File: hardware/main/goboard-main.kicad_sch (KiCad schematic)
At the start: 11 parts, among them J1 USB_C_Receptacle_USB2.0, J2 Conn_02x05_Top_Bottom, J3 Conn_01x01, J4 Conn_01x04, SW11 SW_Push, SW30 SW_DP3T

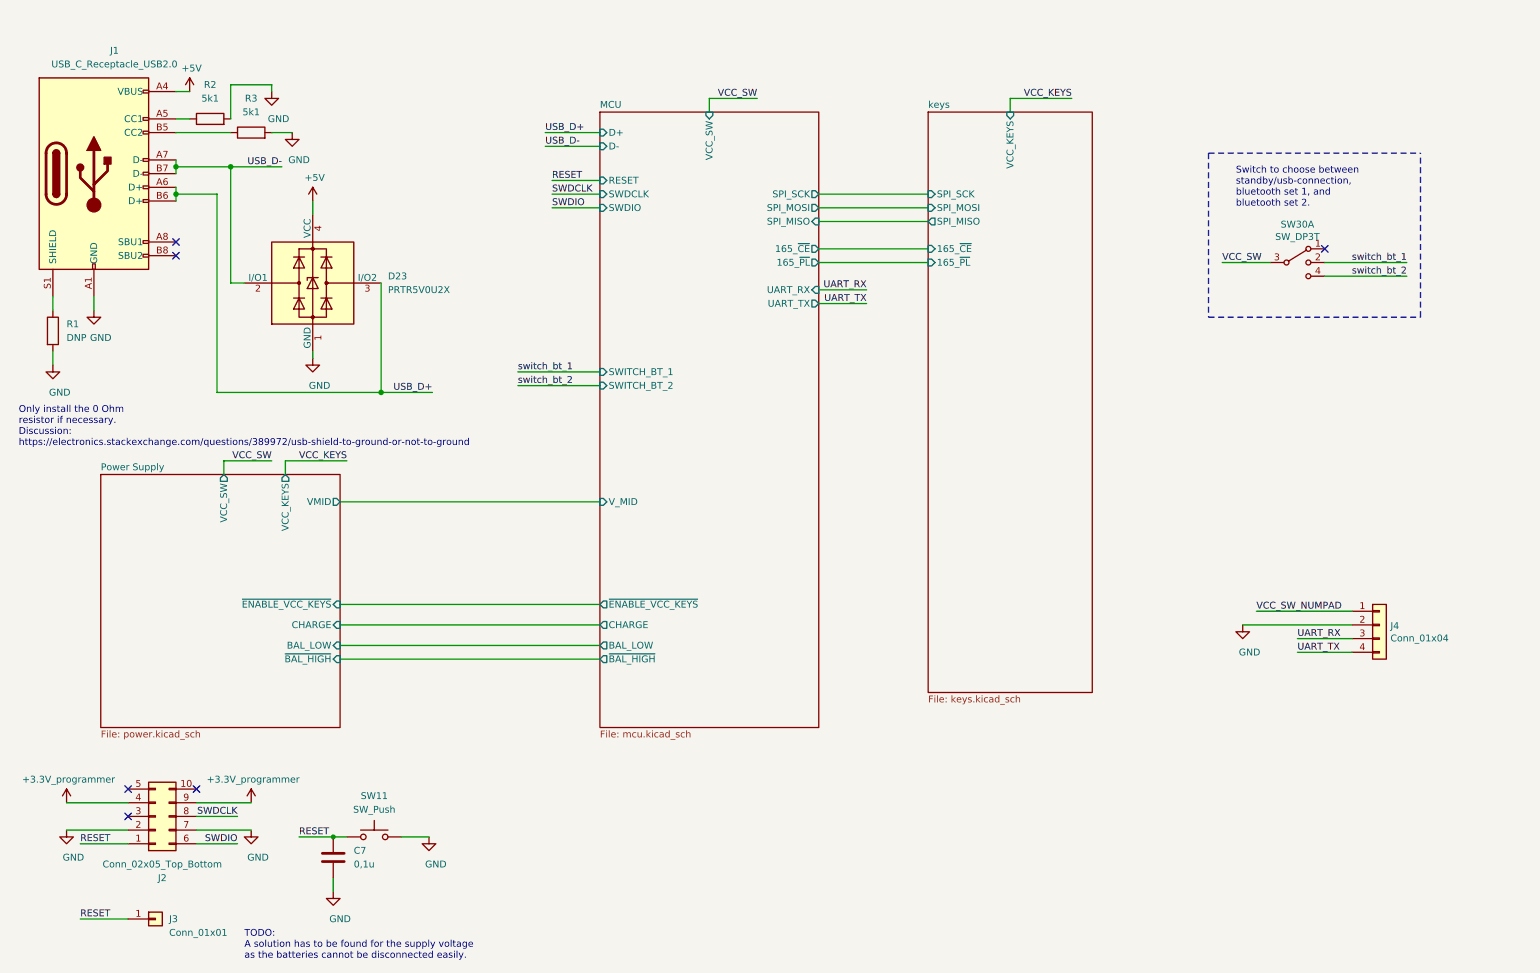
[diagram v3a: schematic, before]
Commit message: Rework the connection to the numpad
Changes:
- The UART lines now have a protection circuit
- The power supply line of the numpad can be switched on and off by the MCU.
- An Id-line is added so that the MCU can detect when the numpad is
  connected.
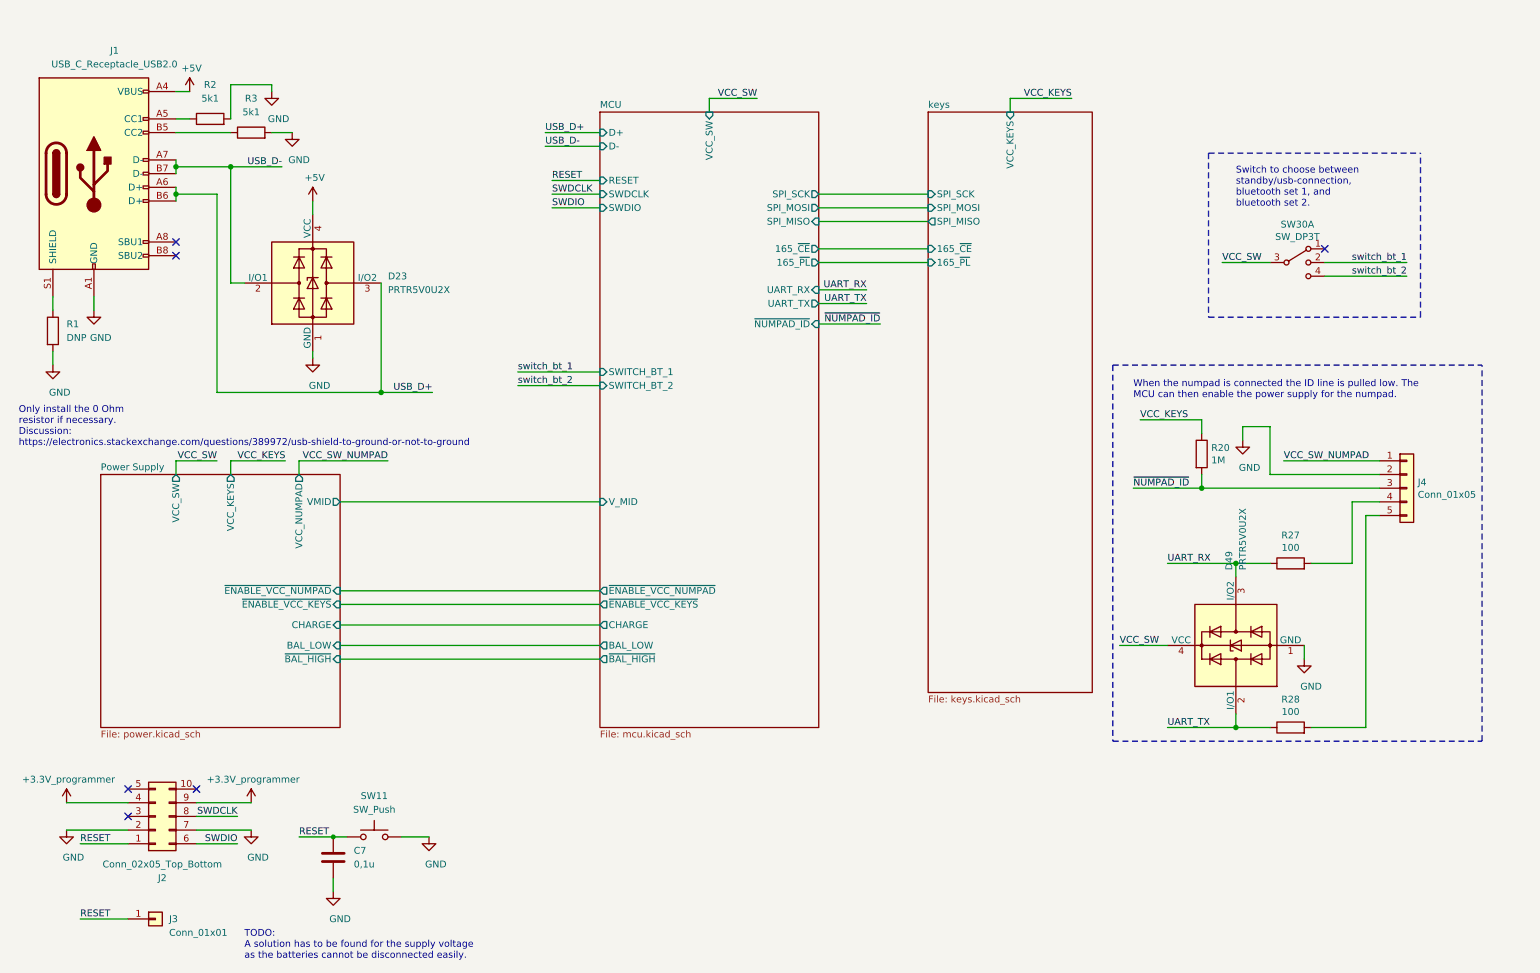
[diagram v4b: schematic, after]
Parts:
- removed J4: Conn_01x04, symbol Connector_Generic:Conn_01x04
- added D49: PRTR5V0U2X, Package_TO_SOT_SMD:SOT-143, symbol Power_Protection:PRTR5V0U2X
- added J4: Conn_01x05, Connector_PinHeader_2.54mm:PinHeader_1x05_P2.54mm_Vertical, symbol Connector_Generic:Conn_01x05
- added R20: 1M, Resistor_SMD:R_0603_1608Metric_Pad0.98x0.95mm_HandSolder, symbol Device:R
- added R27, R28: 100, Resistor_SMD:R_0603_1608Metric_Pad0.98x0.95mm_HandSolder, symbol Device:R
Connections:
- net GND: now also D49.1 (GND), J4.2 (Pin_2)
- net UART_RX: now also D49.3 (I/O2), R27.1
- net UART_TX: now also D49.2 (I/O1), R28.1
- net VCC_KEYS: now also R20.1
- net VCC_SW: now also D49.4 (VCC)
- net VCC_SW_NUMPAD: now also J4.1 (Pin_1)
- new net: J4.4 (Pin_4), R27.2
- new net: J4.5 (Pin_5), R28.2
- new net ~NUMPAD_ID: J4.3 (Pin_3), R20.2
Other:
- sheet MCU ports: added ~ENABLE_VCC_NUMPAD, ~NUMPAD_ID; removed none
- sheet Power Supply ports: added VCC_NUMPAD, ~ENABLE_VCC_NUMPAD; removed none
- note added: "When the numpad is connected the ID line is pulled low. The MCU can then enable the power supply for the numpad."

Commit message: WIP: Design of PCB
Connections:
- net UART_RX: no longer D49.3 (I/O2)
- net UART_TX: no longer D49.2 (I/O1)
- net at J4.4 (Pin_4), R27.2: now also D49.2 (I/O1)
- net at J4.5 (Pin_5), R28.2: now also D49.3 (I/O2)
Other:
- moved on the sheet: D49, R27, R28
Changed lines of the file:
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@@
   (junction (at 80.01 91.44) (diameter 1.016) (color 0 0 0 0))
   (junction (at 232.41 109.22) (diameter 1.016) (color 0 0 0 0))
-  (junction (at 238.76 123.19) (diameter 1.016) (color 0 0 0 0))
-  (junction (at 238.76 153.67) (diameter 1.016) (color 0 0 0 0))
+  (junction (at 246.38 123.19) (diameter 1.016) (color 0 0 0 0))
+  (junction (at 246.38 153.67) (diameter 1.016) (color 0 0 0 0))
   (no_connect (at 33.02 165.1))
   (no_connect (at 33.02 170.18))
@@
     (stroke (width 0) (type solid) (color 0 0 0 0))
   )
-  (wire (pts (xy 217.17 138.43) (xy 226.06 138.43))
-    (stroke (width 0) (type solid) (color 0 0 0 0))
-  )
   (wire (pts (xy 219.71 109.22) (xy 232.41 109.22))
     (stroke (width 0) (type solid) (color 0 0 0 0))
@@
     (stroke (width 0) (type solid) (color 0 0 0 0))
   )
-  (wire (pts (xy 226.06 123.19) (xy 238.76 123.19))
-    (stroke (width 0) (type solid) (color 0 0 0 0))
-  )
-  (wire (pts (xy 226.06 153.67) (xy 238.76 153.67))
+  (wire (pts (xy 226.06 123.19) (xy 236.22 123.19))
+    (stroke (width 0) (type solid) (color 0 0 0 0))
+  )
+  (wire (pts (xy 226.06 138.43) (xy 233.68 138.43))
+    (stroke (width 0) (type solid) (color 0 0 0 0))
+  )
+  (wire (pts (xy 226.06 153.67) (xy 236.22 153.67))
     (stroke (width 0) (type solid) (color 0 0 0 0))
   )
@@
     (stroke (width 0) (type solid) (color 0 0 0 0))
   )
-  (wire (pts (xy 238.76 123.19) (xy 238.76 125.73))
-    (stroke (width 0) (type solid) (color 0 0 0 0))
-  )
-  (wire (pts (xy 238.76 123.19) (xy 245.11 123.19))
-    (stroke (width 0) (type solid) (color 0 0 0 0))
-  )
-  (wire (pts (xy 238.76 151.13) (xy 238.76 153.67))
-    (stroke (width 0) (type solid) (color 0 0 0 0))
-  )
-  (wire (pts (xy 238.76 153.67) (xy 245.11 153.67))
-    (stroke (width 0) (type solid) (color 0 0 0 0))
-  )
   (wire (pts (xy 240.03 97.79) (xy 240.03 100.33))
     (stroke (width 0) (type solid) (color 0 0 0 0))
@@
     (stroke (width 0) (type solid) (color 0 0 0 0))
   )
+  (wire (pts (xy 243.84 123.19) (xy 246.38 123.19))
+    (stroke (width 0) (type solid) (color 0 0 0 0))
+  )
+  (wire (pts (xy 243.84 153.67) (xy 246.38 153.67))
+    (stroke (width 0) (type solid) (color 0 0 0 0))
+  )
   (wire (pts (xy 245.11 97.79) (xy 245.11 106.68))
     (stroke (width 0) (type solid) (color 0 0 0 0))
@@
     (stroke (width 0) (type solid) (color 0 0 0 0))
   )
+  (wire (pts (xy 246.38 123.19) (xy 246.38 125.73))
+    (stroke (width 0) (type solid) (color 0 0 0 0))
+  )
+  (wire (pts (xy 246.38 123.19) (xy 260.35 123.19))
+    (stroke (width 0) (type solid) (color 0 0 0 0))
+  )
+  (wire (pts (xy 246.38 151.13) (xy 246.38 153.67))
+    (stroke (width 0) (type solid) (color 0 0 0 0))
+  )
+  (wire (pts (xy 246.38 153.67) (xy 262.89 153.67))
+    (stroke (width 0) (type solid) (color 0 0 0 0))
+  )
   (wire (pts (xy 247.65 104.14) (xy 265.43 104.14))
     (stroke (width 0) (type solid) (color 0 0 0 0))
   )
-  (wire (pts (xy 251.46 138.43) (xy 251.46 140.97))
-    (stroke (width 0) (type solid) (color 0 0 0 0))
-  )
-  (wire (pts (xy 252.73 123.19) (xy 260.35 123.19))
-    (stroke (width 0) (type solid) (color 0 0 0 0))
-  )
   (wire (pts (xy 255.27 67.31) (xy 270.51 67.31))
     (stroke (width 0) (type solid) (color 0 0 0 0))
@@
     (stroke (width 0) (type solid) (color 0 0 0 0))
   )
+  (wire (pts (xy 259.08 138.43) (xy 259.08 140.97))
+    (stroke (width 0) (type solid) (color 0 0 0 0))
+  )
   (wire (pts (xy 260.35 111.76) (xy 265.43 111.76))
     (stroke (width 0) (type solid) (color 0 0 0 0))
@@
     (stroke (width 0) (type solid) (color 0 0 0 0))
   )
-  (wire (pts (xy 262.89 153.67) (xy 252.73 153.67))
-    (stroke (width 0) (type solid) (color 0 0 0 0))
-  )
   (wire (pts (xy 265.43 114.3) (xy 262.89 114.3))
     (stroke (width 0) (type solid) (color 0 0 0 0))
   )
-  (polyline (pts (xy 215.9 86.36) (xy 215.9 156.21))
+  (polyline (pts (xy 218.44 86.36) (xy 218.44 156.21))
     (stroke (width 0) (type dash) (color 0 0 0 0))
   )
-  (polyline (pts (xy 215.9 86.36) (xy 284.48 86.36))
+  (polyline (pts (xy 218.44 86.36) (xy 284.48 86.36))
     (stroke (width 0) (type dash) (color 0 0 0 0))
   )
-  (polyline (pts (xy 215.9 156.21) (xy 284.48 156.21))
+  (polyline (pts (xy 218.44 156.21) (xy 284.48 156.21))
     (stroke (width 0) (type dash) (color 0 0 0 0))
   )
@@
   )
   (text "When the numpad is connected the ID line is pulled low. The\nMCU can then enable the power supply for the numpad."
-    (at 219.71 92.71 0)
+    (at 220.98 92.71 0)
     (effects (font (size 1.27 1.27)) (justify left bottom))
   )
@@
     (effects (font (size 1.27 1.27)) (justify right bottom))
   )
-  (label "VCC_SW" (at 217.17 138.43 0)
-    (effects (font (size 1.27 1.27)) (justify left bottom))
-  )
   (label "~NUMPAD_ID" (at 219.71 109.22 0)
     (effects (font (size 1.27 1.27)) (justify left bottom))
@@
   )
   (label "UART_RX" (at 226.06 123.19 0)
+    (effects (font (size 1.27 1.27)) (justify left bottom))
+  )
+  (label "VCC_SW" (at 226.06 138.43 0)
     (effects (font (size 1.27 1.27)) (justify left bottom))
   )
@@
     )
   )
-  (symbol (lib_id "power:GND") (at 251.46 140.97 0) (unit 1)
-    (in_bom yes) (on_board yes)
-    (property "Reference" "#PWR0123" (id 0) (at 251.46 147.32 0)
-      (effects (font (size 1.27 1.27)) hide)
-    )
-    (property "Value" "GND" (id 1) (at 252.73 146.05 0))
-    (property "Footprint" "" (id 2) (at 251.46 140.97 0)
-      (effects (font (size 1.27 1.27)) hide)
-    )
-    (property "Datasheet" "" (id 3) (at 251.46 140.97 0)
+  (symbol (lib_id "power:GND") (at 259.08 140.97 0) (unit 1)
+    (in_bom yes) (on_board yes)
+    (property "Reference" "#PWR0123" (id 0) (at 259.08 147.32 0)
+      (effects (font (size 1.27 1.27)) hide)
+    )
+    (property "Value" "GND" (id 1) (at 260.35 146.05 0))
+    (property "Footprint" "" (id 2) (at 259.08 140.97 0)
+      (effects (font (size 1.27 1.27)) hide)
+    )
+    (property "Datasheet" "" (id 3) (at 259.08 140.97 0)
       (effects (font (size 1.27 1.27)) hide)
     )
@@
     )
   )
-  (symbol (lib_id "Device:R") (at 248.92 123.19 90) (unit 1)
-    (in_bom yes) (on_board yes)
-    (property "Reference" "R27" (id 0) (at 248.92 117.9638 90))
-    (property "Value" "100" (id 1) (at 248.92 120.2625 90))
-    (property "Footprint" "Resistor_SMD:R_0603_1608Metric_Pad0.98x0.95mm_HandSolder" (id 2) (at 248.92 124.968 90)
-      (effects (font (size 1.27 1.27)) hide)
-    )
-    (property "Datasheet" "~" (id 3) (at 248.92 123.19 0)
-      (effects (font (size 1.27 1.27)) hide)
-    )
-  )
-  (symbol (lib_id "Device:R") (at 248.92 153.67 90) (unit 1)
-    (in_bom yes) (on_board yes)
-    (property "Reference" "R28" (id 0) (at 248.92 148.4438 90))
-    (property "Value" "100" (id 1) (at 248.92 150.7425 90))
-    (property "Footprint" "Resistor_SMD:R_0603_1608Metric_Pad0.98x0.95mm_HandSolder" (id 2) (at 248.92 155.448 90)
-      (effects (font (size 1.27 1.27)) hide)
-    )
-    (property "Datasheet" "~" (id 3) (at 248.92 153.67 0)
+  (symbol (lib_id "Device:R") (at 240.03 123.19 90) (unit 1)
+    (in_bom yes) (on_board yes)
+    (property "Reference" "R27" (id 0) (at 240.03 117.9638 90))
+    (property "Value" "100" (id 1) (at 240.03 120.2625 90))
+    (property "Footprint" "Resistor_SMD:R_0603_1608Metric_Pad0.98x0.95mm_HandSolder" (id 2) (at 240.03 124.968 90)
+      (effects (font (size 1.27 1.27)) hide)
+    )
+    (property "Datasheet" "~" (id 3) (at 240.03 123.19 0)
+      (effects (font (size 1.27 1.27)) hide)
+    )
+  )
+  (symbol (lib_id "Device:R") (at 240.03 153.67 90) (unit 1)
+    (in_bom yes) (on_board yes)
+    (property "Reference" "R28" (id 0) (at 240.03 148.4438 90))
+    (property "Value" "100" (id 1) (at 240.03 150.7425 90))
+    (property "Footprint" "Resistor_SMD:R_0603_1608Metric_Pad0.98x0.95mm_HandSolder" (id 2) (at 240.03 155.448 90)
+      (effects (font (size 1.27 1.27)) hide)
+    )
+    (property "Datasheet" "~" (id 3) (at 240.03 153.67 0)
       (effects (font (size 1.27 1.27)) hide)
     )
@@
     )
   )
-  (symbol (lib_id "Power_Protection:PRTR5V0U2X") (at 238.76 138.43 90) (unit 1)
-    (in_bom yes) (on_board yes)
-    (property "Reference" "D49" (id 0) (at 237.49 124.46 0)
-      (effects (font (size 1.27 1.27)) (justify left))
-    )
-    (property "Value" "PRTR5V0U2X" (id 1) (at 240.03 124.46 0)
-      (effects (font (size 1.27 1.27)) (justify left))
-    )
-    (property "Footprint" "Package_TO_SOT_SMD:SOT-143" (id 2) (at 238.76 136.906 0)
-      (effects (font (size 1.27 1.27)) hide)
-    )
-    (property "Datasheet" "https://assets.nexperia.com/documents/data-sheet/PRTR5V0U2X.pdf" (id 3) (at 238.76 136.906 0)
-      (effects (font (size 1.27 1.27)) hide)
-    )
-    (property "Mouser" " 771-PRTR5V0U2X-T/R " (id 4) (at 238.76 138.43 0)
-      (effects (font (size 1.27 1.27)) hide)
-    )
-    (property "Part Name" "PRTR5V0U2X,215" (id 5) (at 238.76 138.43 0)
-      (effects (font (size 1.27 1.27)) hide)
-    )
+  (symbol (lib_id "Power_Protection:PRTR5V0U2X") (at 246.38 138.43 90) (mirror x) (unit 1)
+    (in_bom yes) (on_board yes)
+    (property "Reference" "D49" (id 0) (at 245.11 152.4 0)
+      (effects (font (size 1.27 1.27)) (justify left))
+    )
+    (property "Value" "PRTR5V0U2X" (id 1) (at 247.65 152.4 0)
+      (effects (font (size 1.27 1.27)) (justify left))
+    )
+    (property "Footprint" "Package_TO_SOT_SMD:SOT-143" (id 2) (at 246.38 139.954 0)
+      (effects (font (size 1.27 1.27)) hide)
+    )
+    (property "Datasheet" "https://assets.nexperia.com/documents/data-sheet/PRTR5V0U2X.pdf" (id 3) (at 246.38 139.954 0)
+      (effects (font (size 1.27 1.27)) hide)
+    )
+    (property "Mouser" " 771-PRTR5V0U2X-T/R " (id 4) (at 246.38 138.43 0)
+      (effects (font (size 1.27 1.27)) hide)
+    )
+    (property "Part Name" "PRTR5V0U2X,215" (id 5) (at 246.38 138.43 0)
+      (effects (font (size 1.27 1.27)) hide)
+    )

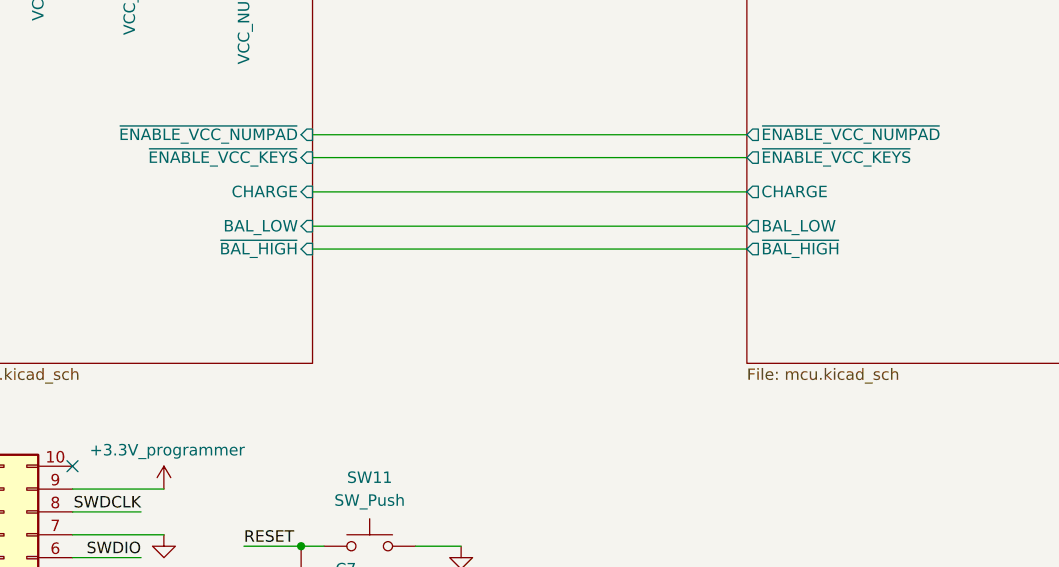
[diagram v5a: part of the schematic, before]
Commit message: Re-add USB voltage sense circuit
Due to firmware limitations the USB voltage cannot be used directly for
waking up the microcontroller.
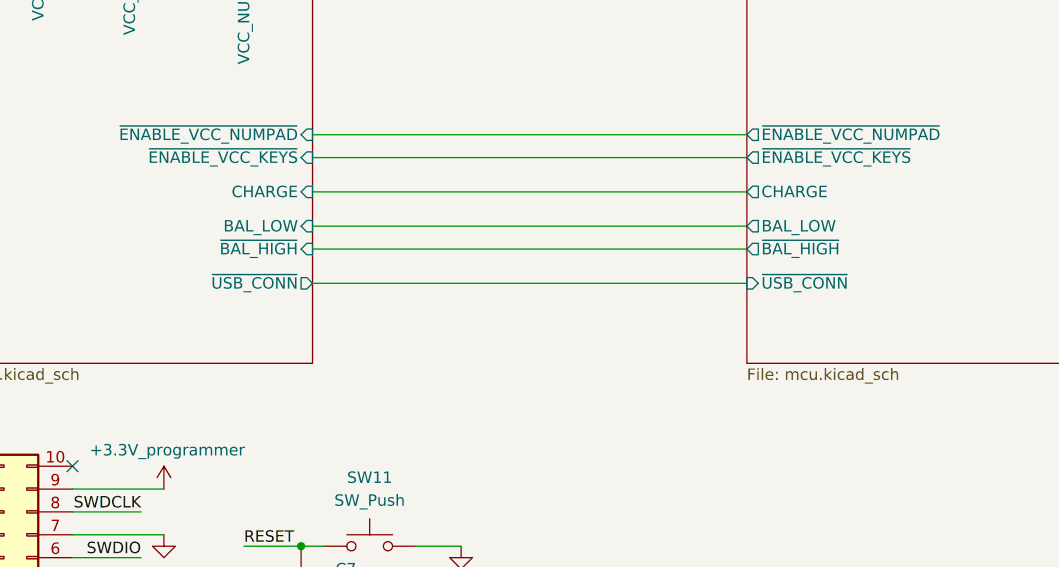
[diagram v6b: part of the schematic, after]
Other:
- sheet MCU ports: added ~USB_CONN; removed none
- sheet Power Supply ports: added ~USB_CONN; removed none
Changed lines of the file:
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@@
+    (stroke (width 0) (type solid) (color 0 0 0 0))
+  )
+  (wire (pts (xy 72.39 144.78) (xy 120.65 144.78))
     (stroke (width 0) (type solid) (color 0 0 0 0))
   )
@@
       (effects (font (size 1.27 1.27)) (justify right))
     )
+    (pin "~USB_CONN" input (at 120.65 144.78 180)
+      (effects (font (size 1.27 1.27)) (justify left))
+    )
   )
   (sheet (at 27.94 106.68) (size 44.45 46.99)
@@
       (effects (font (size 1.27 1.27)) (justify right))
     )
+    (pin "~USB_CONN" output (at 72.39 144.78 0)
+      (effects (font (size 1.27 1.27)) (justify right))
+    )
   )
   (sheet (at 181.61 39.37) (size 30.48 107.7976)
@@
       (reference "#PWR0140") (unit 1) (value "GND") (footprint "")
     )
+    (path "/a2ebbcc0-d455-4794-9fcf-d50cef56d65b/5a4b2b5e-200b-4d68-9e34-c2caa68d1a58"
+      (reference "#PWR?") (unit 1) (value "GND") (footprint "")
+    )
+    (path "/a2ebbcc0-d455-4794-9fcf-d50cef56d65b/94c3f1f0-9419-428a-a6f7-165b4feb93a2"
+      (reference "#PWR?") (unit 1) (value "+3.3V") (footprint "")
+    )
     (path "/a2ebbcc0-d455-4794-9fcf-d50cef56d65b/210515f0-c0f1-4f80-b920-f3ce9df10676"
       (reference "BT1") (unit 1) (value "NiMH") (footprint "Connector_PinHeader_2.54mm:PinHeader_1x02_P2.54mm_Horizontal")
@@
       (reference "Q10") (unit 1) (value "SSM3J338R") (footprint "Package_TO_SOT_SMD:SOT-23_Handsoldering")
     )
+    (path "/a2ebbcc0-d455-4794-9fcf-d50cef56d65b/c7d4bd51-d701-4c56-9708-a98feca559b8"
+      (reference "Q?") (unit 1) (value "BC817") (footprint "Package_TO_SOT_SMD:SOT-23")
+    )
     (path "/a2ebbcc0-d455-4794-9fcf-d50cef56d65b/94b1480c-21b6-4ef7-b592-3977ba8ffc39"
       (reference "R7") (unit 1) (value "10K") (footprint "Resistor_SMD:R_0603_1608Metric")
@@
       (reference "R29") (unit 1) (value "10K") (footprint "Resistor_SMD:R_0603_1608Metric")
     )
+    (path "/a2ebbcc0-d455-4794-9fcf-d50cef56d65b/02993b3e-bd6a-4b6e-8520-b01ae08d0060"
+      (reference "R?") (unit 1) (value "10K") (footprint "Resistor_SMD:R_0603_1608Metric")
+    )
+    (path "/a2ebbcc0-d455-4794-9fcf-d50cef56d65b/f6e90b97-7f06-4011-bca1-7aebee2af537"
+      (reference "R?") (unit 1) (value "4.7K") (footprint "Resistor_SMD:R_0603_1608Metric")
+    )
     (path "/a2ebbcc0-d455-4794-9fcf-d50cef56d65b/fa148395-83b6-415a-8f1a-6bb3d54e1164"
